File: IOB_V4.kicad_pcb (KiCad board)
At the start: 4 copper layers, 80 x 140 mm, 305 parts, among them IC1 PINA350ABSIDDFR, IC10 PINA350ABSIDDFR, IC11 PINA350ABSIDDFR, IC12 PINA350ABSIDDFR, IC2 PINA350ABSIDDFR, IC3 PINA350ABSIDDFR, IC4 PINA350ABSIDDFR, IC5 PINA350ABSIDDFR, IC6 PINA350ABSIDDFR, IC7 PINA350ABSIDDFR, IC8 PINA350ABSIDDFR, IC9 PINA350ABSIDDFR, J1 Conn_01x02, J10 Conn_01x04, J11 Conn_01x04, J12 Conn_01x04, J13 Conn_01x04, J14 Conn_01x04, J15 Conn_01x08, J16 Conn_02x04_Odd_Even, J17 Conn_01x04, J18 Conn_01x10, J19 Conn_01x04, J2 Conn_01x03, J20 Conn_01x10, J3 Conn_01x04, J4 Conn_01x04, J5 Conn_01x04, J6 Conn_01x04, J7 Conn_01x04, J8 Conn_01x04, J9 Conn_01x04, Q1 BSZ0902NSATMA1, Q10 BSZ0902NSATMA1, Q11 BSZ0902NSATMA1, Q12 BSZ0902NSATMA1, Q13 BSZ0902NSATMA1, Q2 BSZ0902NSATMA1, Q3 BSZ0902NSATMA1, Q4 BSZ0902NSATMA1, Q5 BSZ0902NSATMA1, Q6 BSZ0902NSATMA1, Q7 BSZ0902NSATMA1, Q8 BSZ0902NSATMA1, Q9 BSZ0902NSATMA1, SW1 SW_Push_Dual, SW2 SW_Push_Dual, SW3 SW_DIP_x08, U1 REF3033, U14 TS30041, U15 MCP1700-3302E_SOT23, U17 MCP2562FD, U18 W25Q256JV, U19 STM32G474MET3, U2 CD74HC4067SM, X1 TXC-7C

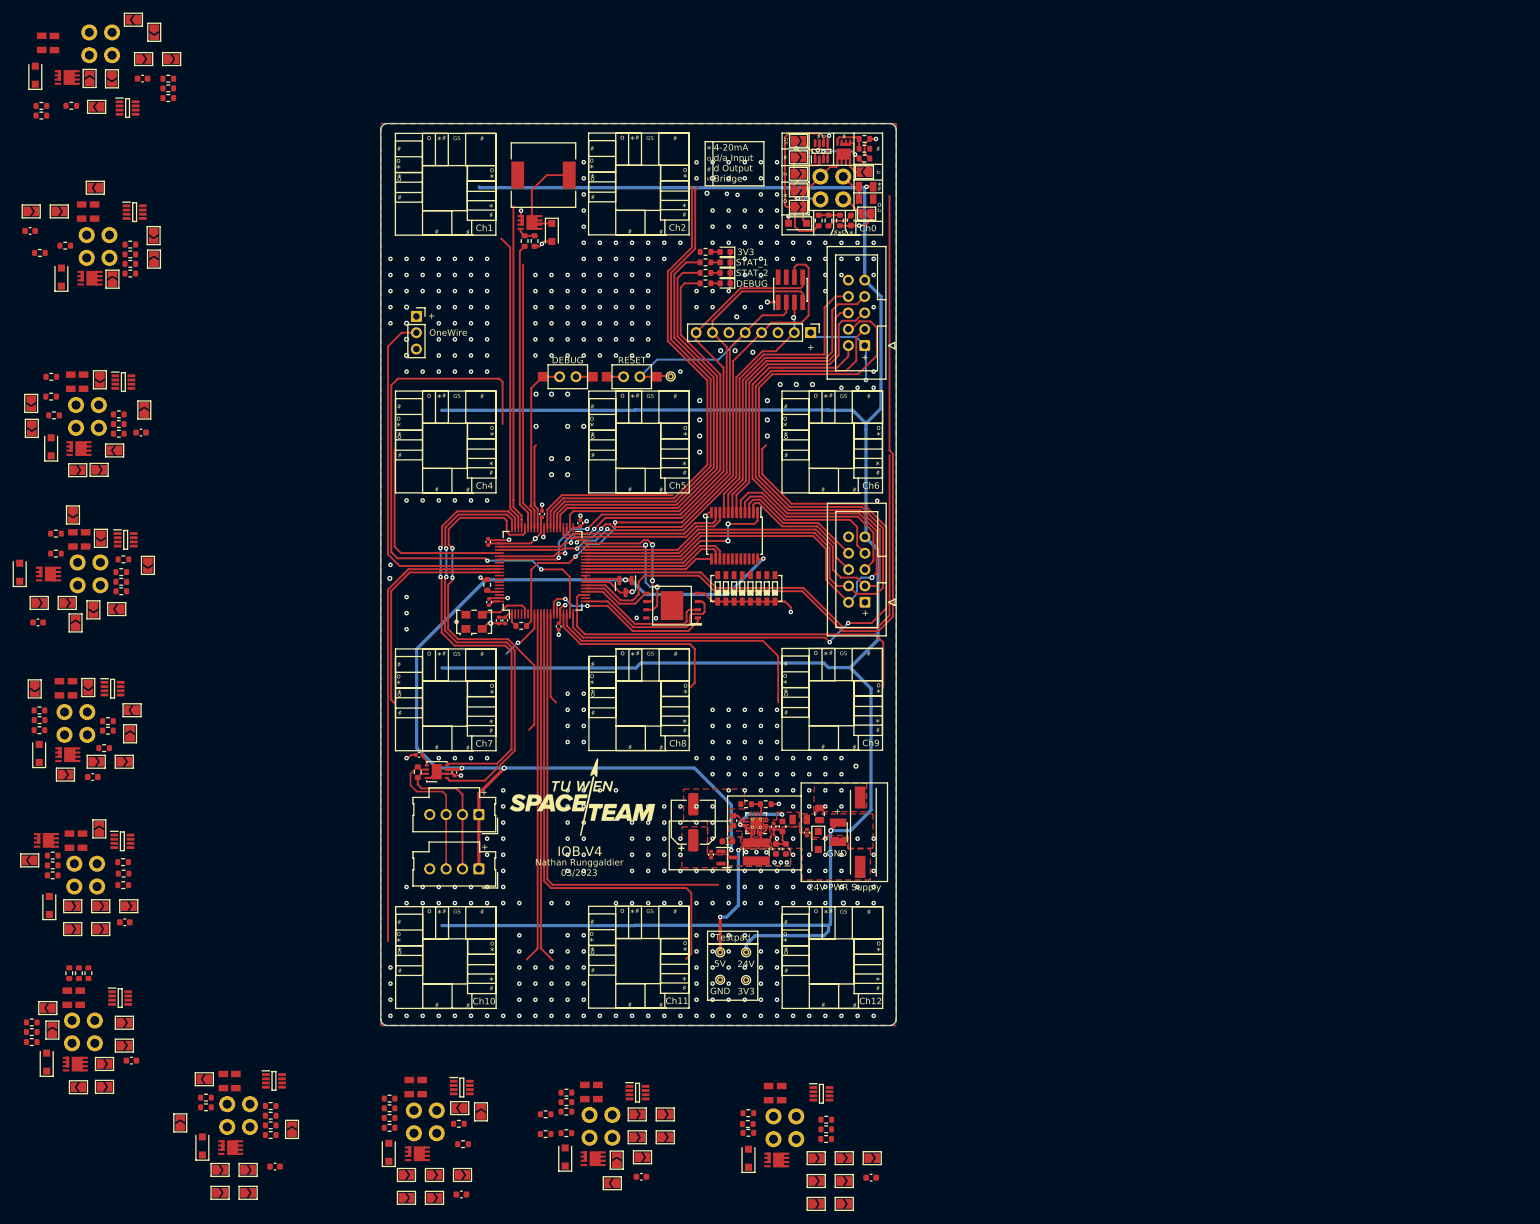
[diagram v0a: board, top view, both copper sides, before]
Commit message: Ch config set, not yet routed
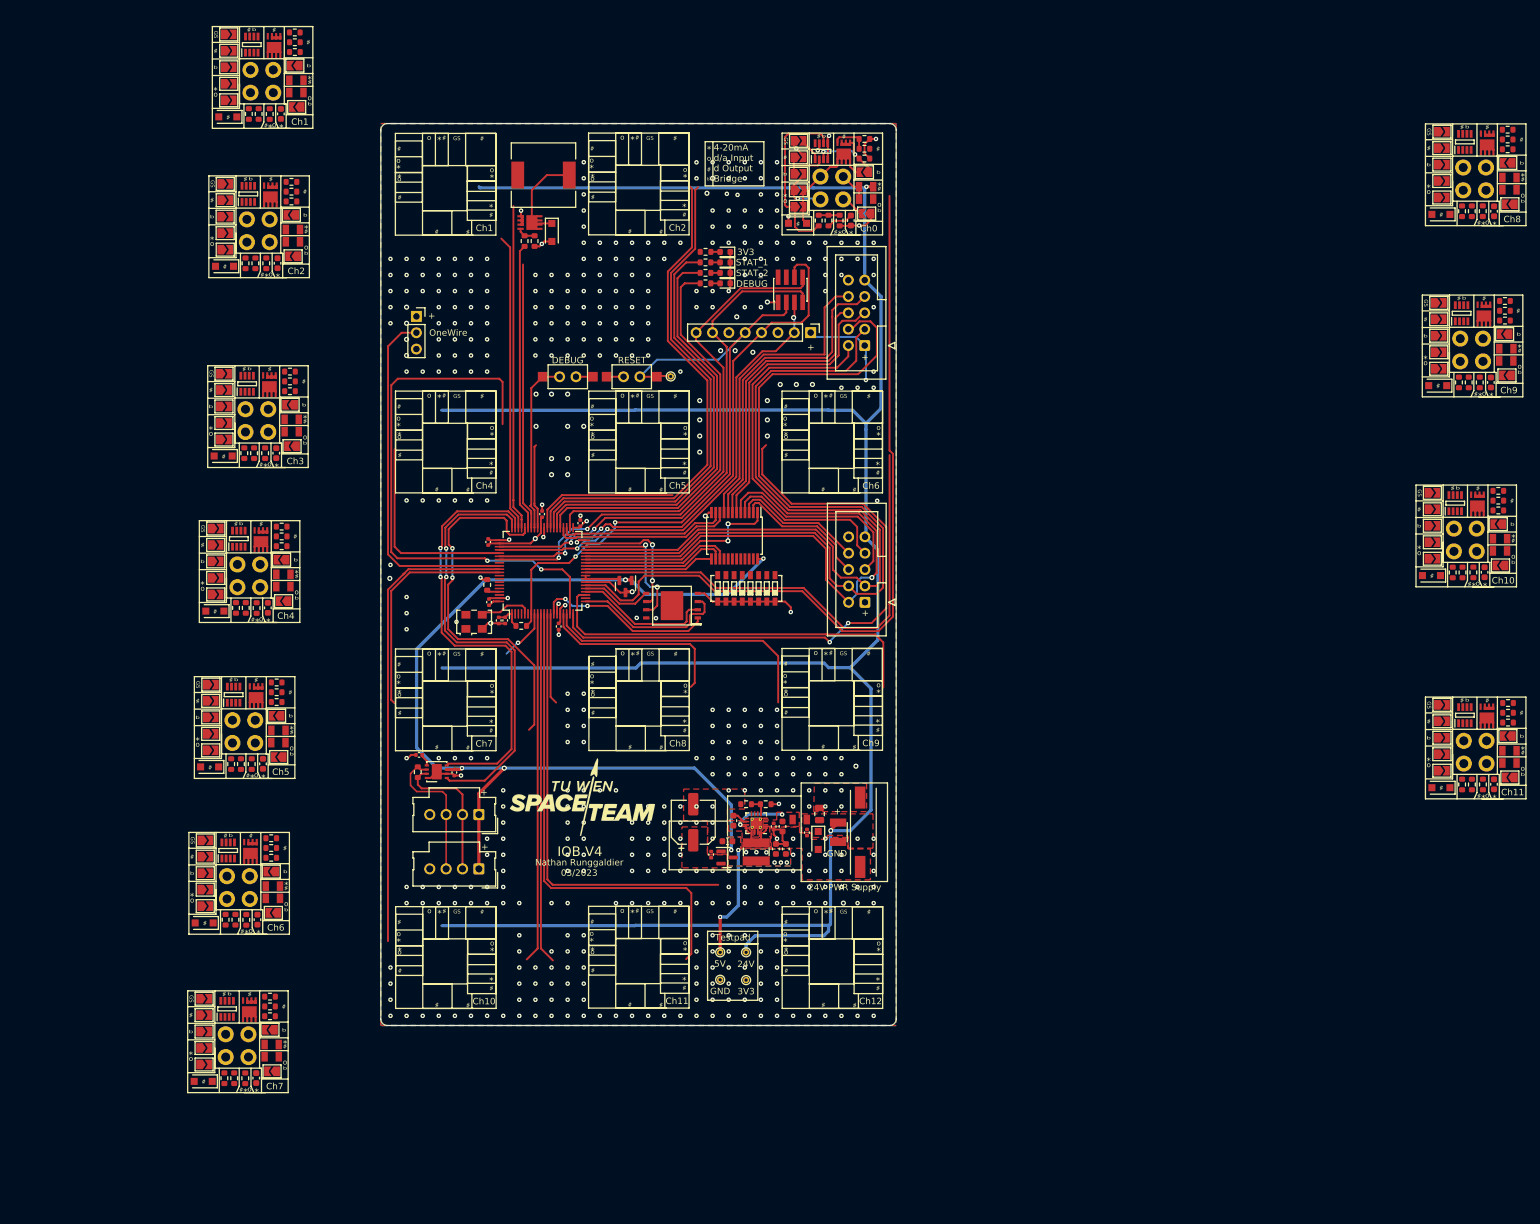
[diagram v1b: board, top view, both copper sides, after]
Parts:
- moved JP52 252.6 mm to (244.9, 36.1), turned to 180 degrees
- moved R46 251.8 mm to (244.9, 32.5), turned to 180 degrees
- moved JP56 250.9 mm to (245.2, 42.5), turned to 180 degrees
- moved R48 250.0 mm to (244.9, 34.0)
- moved Q8 249.8 mm to (241.7, 32.9), turned to -90 degrees
- moved JP53 249.5 mm to (234.7, 33.8)
- moved R47 247.4 mm to (244.9, 30.9), turned to 0 degrees
- moved JP54 244.0 mm to (234.7, 38.9)
- moved F15 244.0 mm to (245.2, 38.4), turned to 0 degrees
- moved F16 241.3 mm to (245.2, 40.3), turned to 0 degrees
- moved J10 240.7 mm to (239.8, 38.6)
- moved D9 240.6 mm to (234.6, 44.1), turned to 180 degrees
- moved C27 240.4 mm to (242.8, 43.6), turned to -90 degrees
- moved JP51 239.0 mm to (234.7, 41.5)
- moved JP55 238.9 mm to (234.7, 36.4), turned to 0 degrees
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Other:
- board text added: "Ch3"
